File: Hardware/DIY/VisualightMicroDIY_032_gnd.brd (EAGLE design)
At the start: 47.4 x 34 mm, 27 parts, among them SW1 SPST_TACT-KMR2, U1 MIC5219 3.3V, U3 ATMEGA32U4, X2 USBPCB, Y1 16MHz

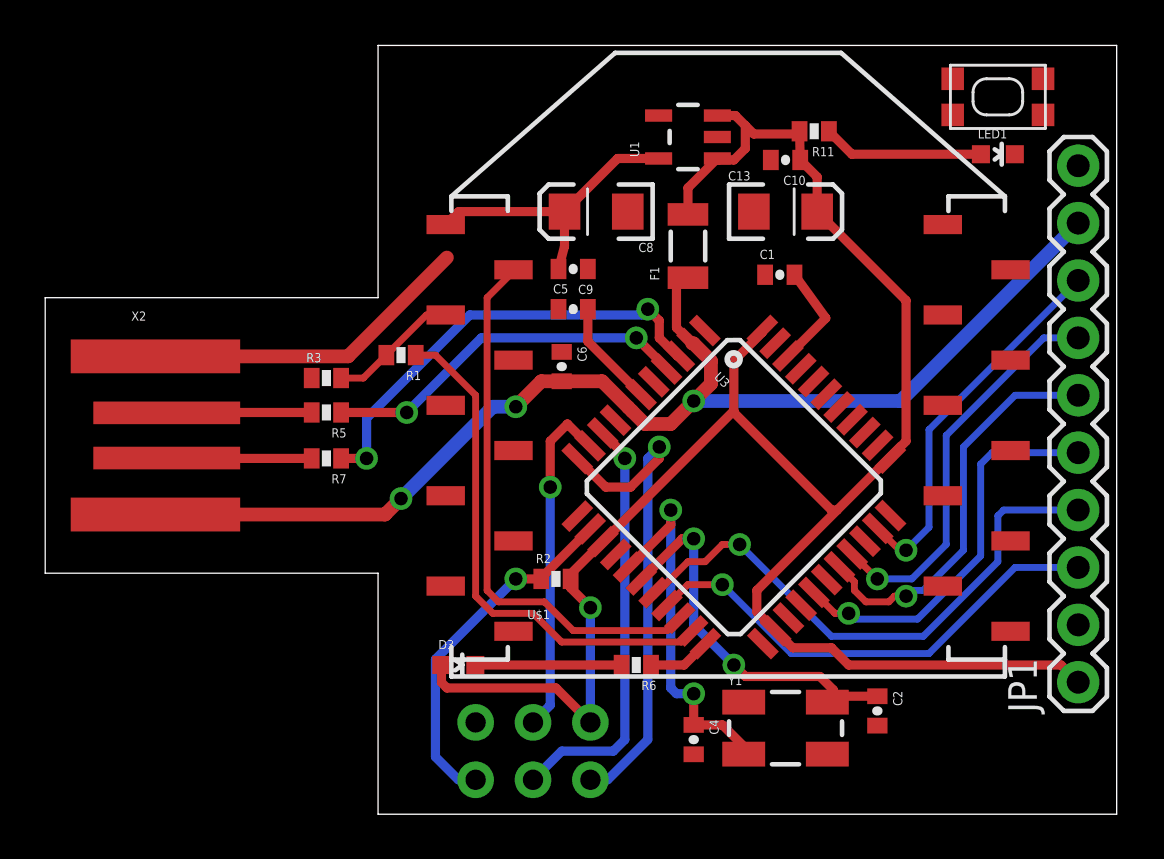
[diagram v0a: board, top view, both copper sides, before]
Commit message: Updates to firmware with MAC address and hardware with ground planes
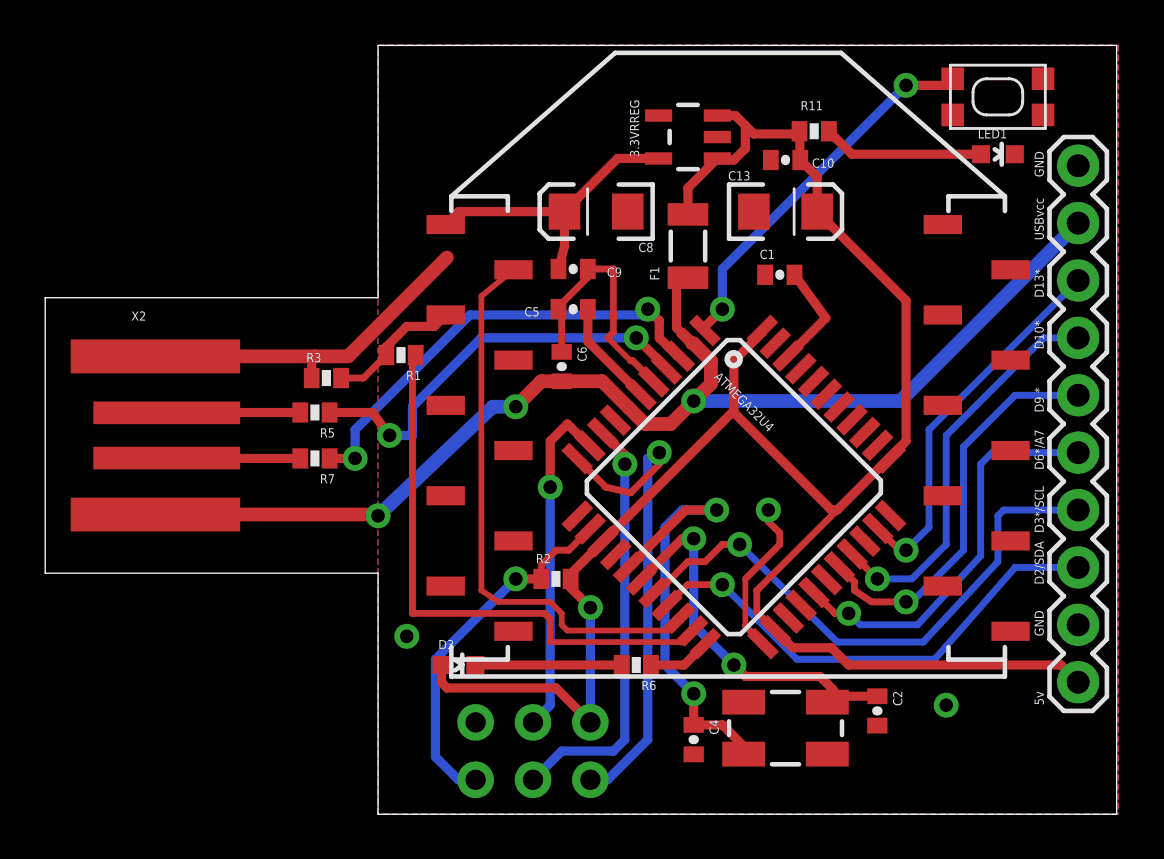
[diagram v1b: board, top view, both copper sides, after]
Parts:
- moved R5 0.51 mm to (37.8, 50.5)
- moved R7 0.51 mm to (37.8, 48.5)
- renumbered U1 to 3.3VRREG, U3 to ATMEGA32U4
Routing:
- net GND: track 14.7 -> 34.1 mm, vias 0 -> 3
- net D7: track 0.00 -> 16.7 mm, vias 0 -> 2
- net N$1: track 16.6 -> 19.8 mm
- net TX: track 22.9 -> 25.3 mm
- net D+: track 16.4 -> 18.5 mm
- net WIFIDOUT: track 24.2 -> 24.8 mm
- net N$8: track 6.42 -> 5.91 mm
- net N$6: track 6.42 -> 5.91 mm
- added copper zone on layer 1, net GND
- added copper zone on layer 16, net GND
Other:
- board text added: "5v"
- board text added: "D10*"
- board text added: "D13*"
- board text added: "D2/SDA"
- board text added: "D3*/SCL"
- board text added: "D6*/A7"
- board text added: "D9 *"
- board text added: "GND"
- board text added: "USBvcc"
